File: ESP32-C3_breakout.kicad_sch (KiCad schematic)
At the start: 26 parts, among them J1 USB4105-GF-A, J2 Conn_01x11_Male, J3 Conn_01x11_Male, SW1 SW_Push, SW2 SW_Push, U1 LD1117S33TR_SOT223, U2 ESP32-C3, U3 WE-TVS-82400102, Y1 40MHz

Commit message: Improved schematics
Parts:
- removed L1: 2nH, symbol Device:L
- added R2: 10k, Resistor_SMD:R_0603_1608Metric, symbol Device:R
- C7, C8: value 10u -> 10p
- SW1, SW2: footprint Button_Switch_SMD:SW_SPST_FSMSM -> Button_Switch_SMD:SW_SPST_PTS810
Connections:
- net +3V3: now also J2.2 (Pin_2), J3.2 (Pin_2), U2.2 (VDD3P3), U2.3 (VDD3P3), R2.1
- net EN: now also J3.3 (Pin_3); no longer J3.1 (Pin_1)
- net GND: now also J2.1 (Pin_1), J2.11 (Pin_11), J3.1 (Pin_1), J3.11 (Pin_11), Y1.1, Y1.3
- net GPIO0: now also J2.3 (Pin_3), U2.4 (XTAL_32K_P/ADC1_CH0); no longer J2.1 (Pin_1)
- net GPIO1: now also J2.4 (Pin_4), U2.5 (XTAL_32K_N/ADC1_CH1); no longer J2.2 (Pin_2)
- net GPIO10: now also J3.9 (Pin_9), U2.16 (GPIO10); no longer J2.11 (Pin_11)
- net GPIO2: now also J2.5 (Pin_5), U2.6 (GPIO2/ADC1_CH2), R2.2; no longer J2.3 (Pin_3)
- net GPIO3: now also J2.6 (Pin_6), U2.8 (GPIO3/ADC1_CH3); no longer J2.4 (Pin_4)
- net GPIO4: now also J2.7 (Pin_7), U2.9 (MTMS/GPIO4/ADC1_CH4); no longer J2.5 (Pin_5)
- net GPIO5: now also J2.8 (Pin_8), U2.10 (MTDI/GPIO5/ADC2_CH0); no longer J2.6 (Pin_6)
- net GPIO6: now also J2.9 (Pin_9), U2.12 (MTCK/GPIO6); no longer J2.7 (Pin_7)
- net GPIO7: now also J3.6 (Pin_6), U2.13 (MTDO/GPIO7); no longer J2.8 (Pin_8)
- net GPIO8: now also J3.7 (Pin_7), R3.2, U2.14 (GPIO8); no longer J2.9 (Pin_9)
- net GPIO9: now also J3.8 (Pin_8); no longer J2.10 (Pin_10)
- net RX: now also J3.4 (Pin_4), U2.27 (U0RXD/GPIO20); no longer J3.2 (Pin_2)
- net TX: now also J3.5 (Pin_5), U2.28 (U0TXD/GPIO21); no longer J3.3 (Pin_3)
- net VDD: now also J2.10 (Pin_10), J3.10 (Pin_10)
- no-connect marks 3 -> 10
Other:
- note added: "?"
- note added: "Blocking Capacitors"
- note added: "Connectors"
- note added: "ES32-C3FN4"
- note added: "Near VDD3P3"
- note added: "Near VDD3P3_CPU"
- note added: "Near VDDA"
- note added: "Pull-Ups"
- title: (none) -> ESP32-C3 Nano
- moved on the sheet: C2, C3, C4, C5, C6, C7, C8, C9, J2, J3, R3, U2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

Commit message: Further improvements
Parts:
- removed U3: WE-TVS-82400102, Package_TO_SOT_SMD:SOT-23-6, symbol Power_Protection:WE-TVS-82400102
- added AE1: Antenna, ESP_Antenna:ESPRESSIF_ESP32_MIFA_2.4GHz_Right, symbol Device:Antenna
- added C13, C14: C, Capacitor_SMD:C_0603_1608Metric, symbol Device:C
- added D1: C4D10120D, Package_TO_SOT_SMD:SOT-223, symbol Diode:C4D10120D
- added L1: L, Inductor_SMD:L_0603_1608Metric, symbol Device:L
- added R6, R7: 22R, Resistor_SMD:R_0603_1608Metric, symbol Device:R
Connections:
- net +3V3: no longer J2.2 (Pin_2)
- net ANT: now also C13.1, L1.1
- net GND: now also J2.10 (Pin_10), J2.2 (Pin_2), J3.10 (Pin_10), C13.2, C14.2; no longer J2.11 (Pin_11), J3.11 (Pin_11)
- net GPIO0: now also J3.4 (Pin_4); no longer J2.3 (Pin_3)
- net GPIO1: now also J3.5 (Pin_5); no longer J2.4 (Pin_4)
- net GPIO10: now also J2.5 (Pin_5); no longer J3.9 (Pin_9)
- net GPIO2: now also J3.6 (Pin_6); no longer J2.5 (Pin_5)
- net GPIO3: now also J3.7 (Pin_7); no longer J2.6 (Pin_6)
- net GPIO4: now also J3.8 (Pin_8); no longer J2.7 (Pin_7)
- net GPIO5: now also J3.9 (Pin_9); no longer J2.8 (Pin_8)
- net GPIO7: now also J2.8 (Pin_8); no longer J3.6 (Pin_6)
- net GPIO8: now also J2.7 (Pin_7); no longer J3.7 (Pin_7)
- net GPIO9: now also J2.6 (Pin_6); no longer J3.8 (Pin_8)
- net RX: now also J2.4 (Pin_4); no longer J3.4 (Pin_4)
- net TX: now also J2.3 (Pin_3); no longer J3.5 (Pin_5)
- net USB_D+: now also R7.2
- net USB_D-: now also R6.2
- net VDD: now also D1.2 (K); no longer J1.A4_B9 (VBUS), J1.B4_A9 (VBUS), J2.10 (Pin_10), J3.10 (Pin_10)
- net D_P: now reaches J1.A6 (DP1), J1.B6 (DP2)
- net D_P: now also R7.1
- net D_N: now reaches J1.A7 (DN1), J1.B7 (DN2)
- net D_N: now also R6.1
- new net: AE1.1 (A), C14.1, L1.2
- new net USB_+5V: D1.1 (A1), J1.A4_B9 (VBUS), J1.B4_A9 (VBUS), J3.11 (Pin_11)
- new net VIN: D1.3 (A2), J2.11 (Pin_11)

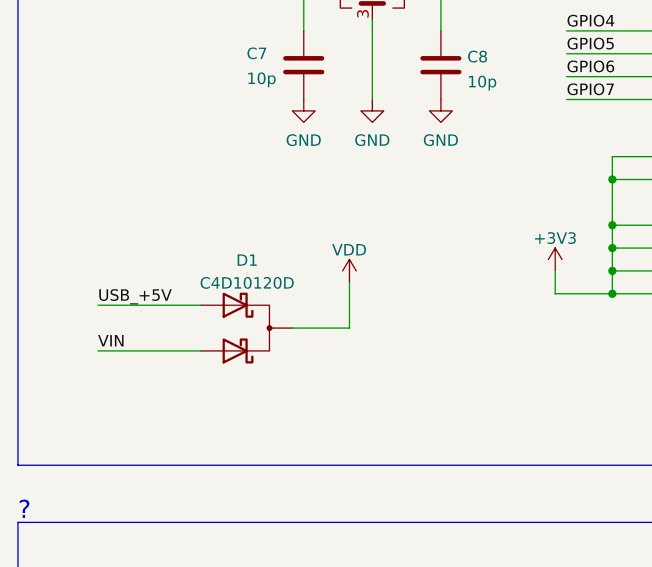
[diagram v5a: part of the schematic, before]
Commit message: add: datasheets, distributors
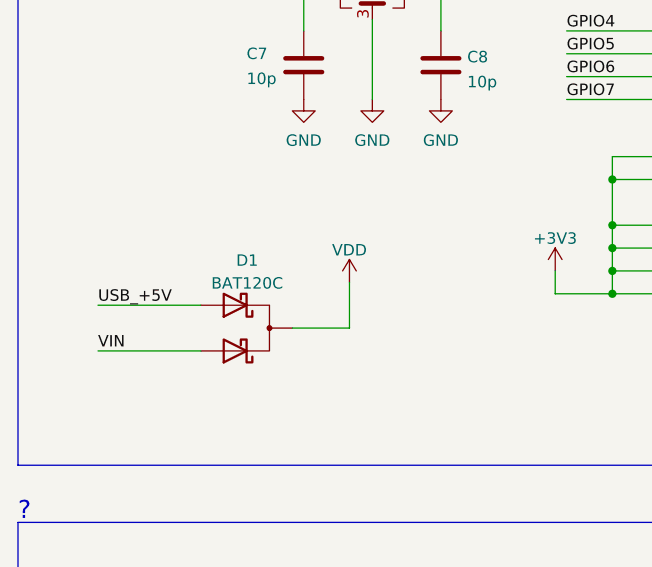
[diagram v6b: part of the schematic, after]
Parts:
- C1, C11, C5: Distributor (none) -> https://www.tme.eu/cz/details/cl10a105kp8nnnc/kondenzatory-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
- C10, C12, C3, C4: Distributor (none) -> https://www.tme.eu/cz/details/cl10a106mq8nnnc/kondenzatory-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
- C2, C6, C9: Distributor (none) -> https://www.tme.eu/cz/details/cl10b104kb8nnnc/kondenzatory-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
- C7, C8: Distributor (none) -> https://www.tme.eu/cz/details/cl10c100jb8nnnc/kondenzatory-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
- D1: value C4D10120D -> BAT120C; Field4 (none) -> https://cz.mouser.com/ProductDetail/Nexperia/BAT120C115?qs=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
- J1: Distributor (none) -> https://cz.mouser.com/ProductDetail/GCT/USB4105-GF-A?qs=KUo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
- R1, R2, R3: Distributor (none) -> https://www.tme.eu/cz/details/smd0603-10k-1%25/rezistory-sm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
- R4, R7: Distributor (none) -> https://www.tme.eu/Document/b315665a56acbc42df513c99b390ad9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
- R5: Distributor (none) -> https://www.tme.eu/cz/details/smd0603-5k1-1%25/rezistory-sm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
- R6: Distributor (none) -> https://www.tme.eu/cz/details/smd0603-22r-1%25/rezistory-sm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
- SW1, SW2: Distributor (none) -> https://www.tme.eu/cz/details/pts830gm140smtrlfs/mikrospina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
- U2: Distributor (none) -> https://www.tme.eu/cz/details/esp32c3/moduly-iot-wifi-bluet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
- Y1: Distributor (none) -> https://cz.mouser.com/ProductDetail/ECS/ECS-400-8-37B2-CWY-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

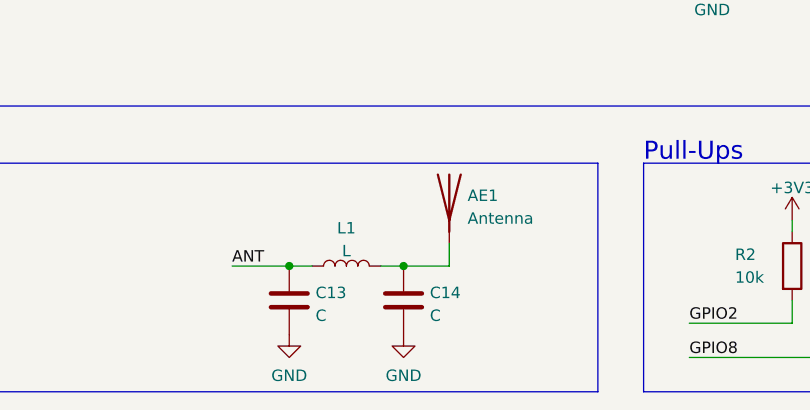
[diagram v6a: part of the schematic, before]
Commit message: add: antenna π matching network values
values, datasheets, distributors
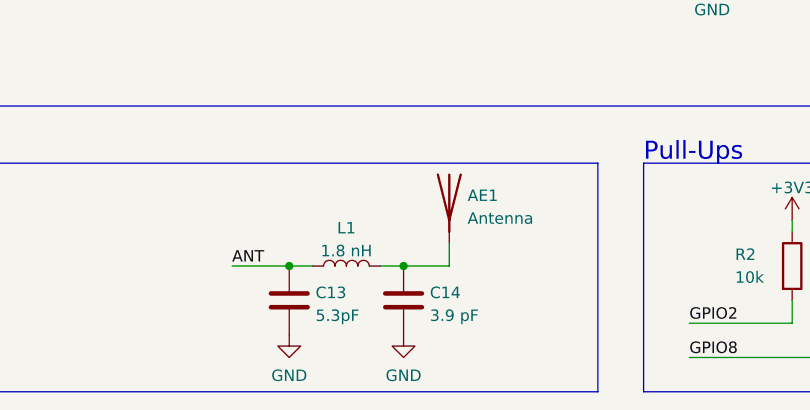
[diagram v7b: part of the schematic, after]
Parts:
- C13: value C -> 5.3pF; Distributor (none) -> https://cz.mouser.com/ProductDetail/Murata-Electronics/GCM1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
- C14: value C -> 3.9 pF; Distributor (none) -> https://cz.mouser.com/ProductDetail/Murata-Electronics/GRM1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
- L1: value L -> 1.8 nH; Distributor (none) -> https://cz.mouser.com/ProductDetail/Murata-Electronics/LQW1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
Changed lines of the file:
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@@
       (effects (font (size 1.27 1.27)) (justify left))
     )
-    (property "Value" "C" (id 1) (at 117.221 185.8522 0)
+    (property "Value" "3.9 pF" (id 1) (at 117.221 185.8522 0)
       (effects (font (size 1.27 1.27)) (justify left))
     )
@@
       (effects (font (size 1.27 1.27)) hide)
     )
-    (property "Datasheet" "~" (id 3) (at 114.3 184.15 0)
+    (property "Datasheet" "https://cz.mouser.com/datasheet/2/281/1/GRM1885C2A3R9BA01_01A-1985303.pdf" (id 3) (at 114.3 184.15 0)
+      (effects (font (size 1.27 1.27)) hide)
+    )
+    (property "Distributor" "https://cz.mouser.com/ProductDetail/Murata-Electronics/GRM1885C2A3R9BA01D?qs=4W3PNmGdEWEmpDv2WaSz6Q%3D%3D" (id 4) (at 114.3 184.15 0)
       (effects (font (size 1.27 1.27)) hide)
     )
@@
       (effects (font (size 1.27 1.27)) (justify left))
     )
-    (property "Value" "C" (id 1) (at 104.521 185.8522 0)
+    (property "Value" "5.3pF" (id 1) (at 104.521 185.8522 0)
       (effects (font (size 1.27 1.27)) (justify left))
     )
@@
       (effects (font (size 1.27 1.27)) hide)
     )
-    (property "Datasheet" "~" (id 3) (at 101.6 184.15 0)
+    (property "Datasheet" "https://cz.mouser.com/datasheet/2/281/GCM1885C1H5R3BA16_01-1965865.pdf" (id 3) (at 101.6 184.15 0)
+      (effects (font (size 1.27 1.27)) hide)
+    )
+    (property "Distributor" "https://cz.mouser.com/ProductDetail/Murata-Electronics/GCM1885C1H5R3BA16D?qs=QzBtWTOodeXo%2FHeCEuhFGA%3D%3D" (id 4) (at 101.6 184.15 0)
       (effects (font (size 1.27 1.27)) hide)
     )
@@
     (in_bom yes) (on_board yes) (fields_autoplaced)
     (property "Reference" "L1" (id 0) (at 107.95 176.1322 90))
-    (property "Value" "L" (id 1) (at 107.95 178.6691 90))
+    (property "Value" "1.8 nH" (id 1) (at 107.95 178.6691 90))
     (property "Footprint" "Inductor_SMD:L_0603_1608Metric" (id 2) (at 107.95 180.34 0)
       (effects (font (size 1.27 1.27)) hide)
     )
-    (property "Datasheet" "~" (id 3) (at 107.95 180.34 0)
+    (property "Datasheet" "https://cz.mouser.com/datasheet/2/281/JELF243A_9139-1699565.pdf" (id 3) (at 107.95 180.34 0)
+      (effects (font (size 1.27 1.27)) hide)
+    )
+    (property "Distributor" "https://cz.mouser.com/ProductDetail/Murata-Electronics/LQW18AS1N8J0ZD?qs=Mv7BduZupUjHep4tpVVZaA%3D%3D" (id 4) (at 107.95 180.34 90)
       (effects (font (size 1.27 1.27)) hide)
     )
@@
     )
     (path "/39e5b5a2-35d0-40e3-8897-88a054f19a0d"
-      (reference "C13") (unit 1) (value "C") (footprint "Capacitor_SMD:C_0603_1608Metric")
+      (reference "C13") (unit 1) (value "5.3pF") (footprint "Capacitor_SMD:C_0603_1608Metric")
     )
     (path "/1091aee0-9629-4e12-beb8-6cde10ce23c9"
-      (reference "C14") (unit 1) (value "C") (footprint "Capacitor_SMD:C_0603_1608Metric")
+      (reference "C14") (unit 1) (value "3.9 pF") (footprint "Capacitor_SMD:C_0603_1608Metric")
     )
     (path "/f86f60c4-f78e-48f1-a3fb-712348c381dd"
@@
     )
     (path "/e2d46498-a020-4c6b-88dc-ea3990b76feb"
-      (reference "L1") (unit 1) (value "L") (footprint "Inductor_SMD:L_0603_1608Metric")
+      (reference "L1") (unit 1) (value "1.8 nH") (footprint "Inductor_SMD:L_0603_1608Metric")
     )
     (path "/2c4c6883-9699-4569-b514-c570bee3e9c2"

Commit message: edit: ESP32C3FH4 distributor
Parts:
- U2: Distributor https://www.tme.eu/cz/details/esp32c3/moduly-iot-wifi-bluet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 -> https://cz.mouser.com/ProductDetail/Espressif-Systems/ESP32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
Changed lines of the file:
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@@
       (effects (font (size 1.27 1.27)) hide)
     )
-    (property "Distributor" "https://www.tme.eu/cz/details/esp32c3/moduly-iot-wifi-bluetooth/espressif/esp32-c3/" (id 4) (at 116.84 119.38 0)
+    (property "Distributor" "https://cz.mouser.com/ProductDetail/Espressif-Systems/ESP32-C3FH4?qs=iLbezkQI%252BsgL5PSvEueYlQ%3D%3D" (id 4) (at 116.84 119.38 0)
       (effects (font (size 1.27 1.27)) hide)
     )
